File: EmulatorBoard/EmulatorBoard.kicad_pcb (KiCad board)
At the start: 2 copper layers, 106.9 x 59.3 mm, 25 parts, among them J2 Screw_Terminal_01x10, J3 Screw_Terminal_01x02, Q1 BC338, Q2 IRF740, Q3 IRF740, Q4 IRF740, Q5 IRF740, Q6 BC338, U1 TC4424, U2 TC4424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

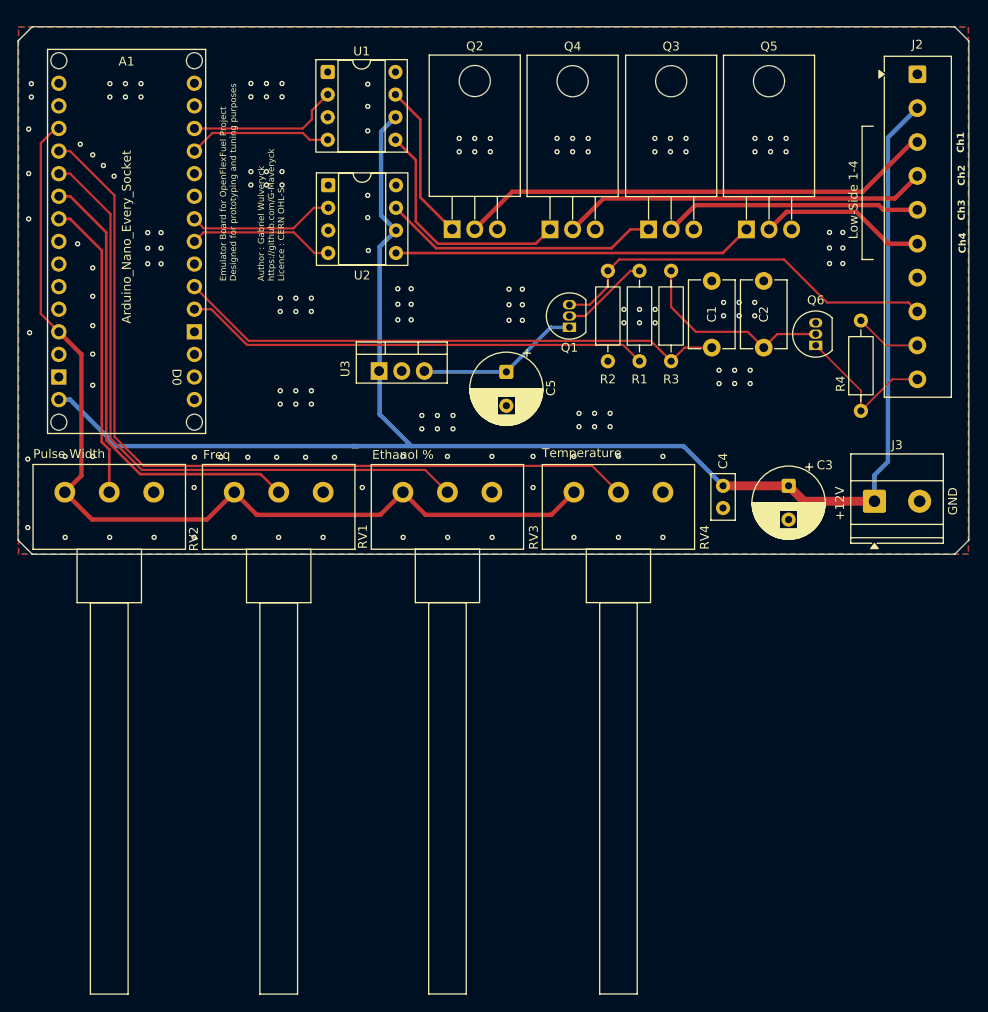
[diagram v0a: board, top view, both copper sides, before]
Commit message: Updated and sourced EmulatoBoard (DevBoard)
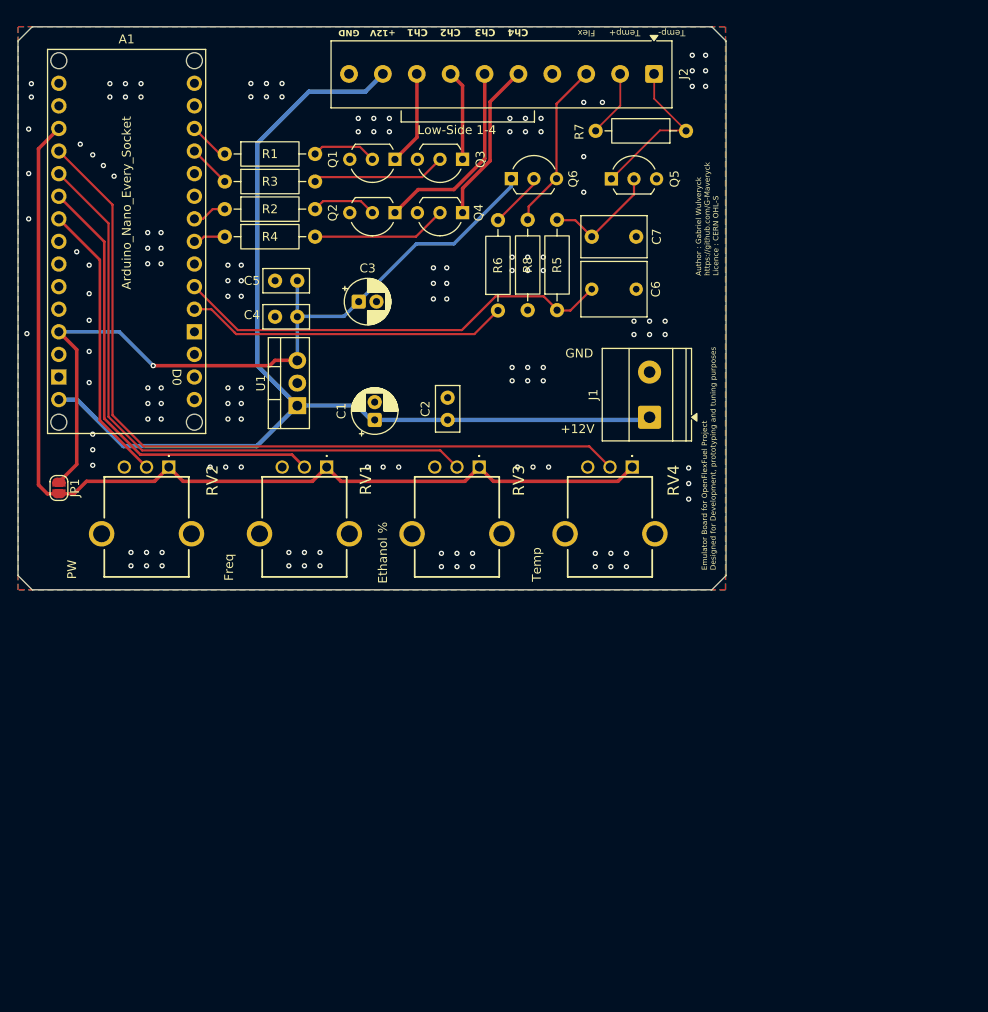
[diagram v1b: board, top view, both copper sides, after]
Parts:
- removed J3: Screw_Terminal_01x02, TerminalBlock_Phoenix:TerminalBlock_Phoenix_MKDS-1,5-2-5.08_1x02_P5.08mm_Horizontal
- removed the RV1 at (66.7, 97.0)
- removed U2: TC4424, Package_DIP:DIP-8_W7.62mm_Socket
- removed U3: LM7805_TO220, Package_TO_SOT_THT:TO-220-3_Vertical
- added C1: 10uF, Capacitor_THT:CP_Radial_D5.0mm_P2.00mm, F.Cu at (82.5, 88.9)
- added C2: 1nF, Capacitor_THT:C_Disc_D5.0mm_W2.5mm_P2.50mm, F.Cu at (90.7, 88.9)
- added J1: Screw_Terminal_01x02, TerminalBlock_Phoenix:TerminalBlock_Phoenix_MKDS-1,5-2-5.08_1x02_P5.08mm_Horizontal, F.Cu at (113.4, 88.6)
- added JP1: SolderJumper_2_Open, Jumper:SolderJumper-2_P1.3mm_Open_RoundedPad1.0x1.5mm, F.Cu at (47.0, 96.5)
- added R1: 1k, Resistor_THT:R_Axial_DIN0207_L6.3mm_D2.5mm_P10.16mm_Horizontal, F.Cu at (65.6, 59.0)
- added R5: 1k, Resistor_THT:R_Axial_DIN0207_L6.3mm_D2.5mm_P10.16mm_Horizontal, F.Cu at (103.0, 76.6)
- added R7: 1k, Resistor_THT:R_Axial_DIN0207_L6.3mm_D2.5mm_P10.16mm_Horizontal, F.Cu at (117.5, 56.4)
- added R8: 1k, Resistor_THT:R_Axial_DIN0207_L6.3mm_D2.5mm_P10.16mm_Horizontal, F.Cu at (99.7, 76.6)
- added RV4: 100k Lin, OpenFlex_FootPrint_Lib:PTN091V100115K1B, F.Cu at (108.5, 100.2)
- C3: footprint Capacitor_THT:CP_Radial_D8.0mm_P3.80mm -> Capacitor_THT:CP_Radial_D5.0mm_P2.00mm
- C5: value 10uF -> 100nF; footprint Capacitor_THT:CP_Radial_D8.0mm_P3.80mm -> Capacitor_THT:C_Disc_D5.0mm_W2.5mm_P2.50mm
- C6: renamed from C1; footprint Capacitor_THT:C_Disc_D7.5mm_W5.0mm_P7.50mm -> Capacitor_THT:C_Rect_L7.2mm_W6.0mm_P5.00mm
- C7: renamed from C2; footprint Capacitor_THT:C_Disc_D7.5mm_W5.0mm_P7.50mm -> Capacitor_THT:C_Rect_L7.2mm_W4.5mm_P5.00mm_FKS2_FKP2_MKS2_MKP2
- Q1, Q6: value BC338 -> 2N2222A; footprint Package_TO_SOT_THT:TO-92_Inline -> Package_TO_SOT_THT:TO-92L_Inline_Wide
- Q2, Q3, Q4, Q5: value IRF740 -> 2N2222A; footprint Package_TO_SOT_THT:TO-220-3_Horizontal_TabDown -> Package_TO_SOT_THT:TO-92L_Inline_Wide
- RV1: renamed from RV4; footprint Potentiometer_THT:Potentiometer_Omeg_PC16BU_Horizontal -> OpenFlex_FootPrint_Lib:PTN091V100115K1B
- RV2, RV3: footprint Potentiometer_THT:Potentiometer_Omeg_PC16BU_Horizontal -> OpenFlex_FootPrint_Lib:PTN091V100115K1B
- U1: value TC4424 -> LM7805_TO220; footprint Package_DIP:DIP-8_W7.62mm_Socket -> Package_TO_SOT_THT:TO-220-3_Vertical
- moved R4 74.2 mm to (65.6, 68.3), turned to 0 degrees
- moved R3 54.1 mm to (65.6, 62.1), turned to 0 degrees
- moved C3 52.6 mm to (80.7, 75.6), turned to 0 degrees
- moved C4 51.5 mm to (73.8, 77.3), turned to 180 degrees
- moved R2 46.3 mm to (65.6, 65.2), turned to 0 degrees
- moved Q6 39.0 mm to (97.9, 61.8), turned to 0 degrees
- moved U1 37.7 mm to (73.8, 87.3), turned to 90 degrees
- moved RV1 31.0 mm to (74.1, 100.2), turned to 180 degrees
- moved J2 29.6 mm to (113.9, 50.0), turned to 180 degrees
- moved Q1 27.2 mm to (84.8, 59.6), turned to 180 degrees
- moved C5 25.6 mm to (73.8, 73.2), turned to 180 degrees
- moved C7 23.0 mm to (106.9, 68.3), turned to 0 degrees
- moved Q3 22.3 mm to (92.4, 59.6), turned to 180 degrees
- moved R6 16.9 mm to (96.4, 76.6)
- moved Q5 16.2 mm to (109.1, 61.8)
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- renumbered R1 to R6
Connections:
- A1 pad 5V: +5V -> VDD
- A1 pad AREF: +5V -> /AREF_Pin
- C3 pad 1: +12V -> VDD
- C4 pad 1: +12V -> VDD
- C7 pad 1: Net-(Q6-B) -> Net-(Q5-B)
- J2 pad 1: GND -> Temp_-
- J2 pad 10: Temp_- -> GND
- J2 pad 2: +12V -> Temp_+
- J2 pad 3: /INJ_CH1 -> Flex_SNSR_Signal
- J2 pad 4: /INJ_CH2 -> unconnected-(J2-Pin_4-Pad4)
- J2 pad 5: /INJ_CH3 -> /INJ_CH4
- J2 pad 6: /INJ_CH4 -> /INJ_CH3
- J2 pad 7: unconnected-(J2-Pin_7-Pad7) -> /INJ_CH2
- J2 pad 8: Flex_SNSR_Signal -> /INJ_CH1
- J2 pad 9: Temp_+ -> +12V
- Q1 pad 1: VDD -> /INJ_CH1
- Q1 pad 3: Flex_SNSR_Signal -> GND
- Q2 pad 1: Net-(Q2-G) -> /INJ_CH3
- Q2 pad 2: /INJ_CH1 -> Net-(Q2-B)
- Q3 pad 1: Net-(Q3-G) -> /INJ_CH2
- Q3 pad 2: /INJ_CH3 -> Net-(Q3-B)
- Q4 pad 1: Net-(Q4-G) -> /INJ_CH4
- Q4 pad 2: /INJ_CH2 -> Net-(Q4-B)
- Q5 pad 1: Net-(Q5-G) -> Temp_-
- Q5 pad 2: /INJ_CH4 -> Net-(Q5-B)
- Q6 pad 1: Temp_- -> VDD
- Q6 pad 3: GND -> Flex_SNSR_Signal
- R2 pad 1: GND -> /GD_CH3
- R2 pad 2: Flex_SNSR_Signal -> Net-(Q2-B)
- R3 pad 1: /MCU_D3 -> /GD_CH2
- R3 pad 2: Net-(Q6-B) -> Net-(Q3-B)
- R4 pad 1: Temp_- -> /GD_CH4
- R4 pad 2: Temp_+ -> Net-(Q4-B)
- R6 pad 2: Net-(Q1-B) -> Net-(Q6-B)
- RV1 pad 1: +5V -> /AREF_Pin
- RV1 pad 2: /Temp_Pot -> /FREQ_Pot
- RV2 pad 1: +5V -> /AREF_Pin
- RV3 pad 1: +5V -> /AREF_Pin
- U1 pad 1: unconnected-(U1-NC-Pad1) -> +12V
- U1 pad 2: /GD_CH1 -> GND
- U1 pad 3: GND -> VDD
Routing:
- net /AREF_Pin: track 0.00 -> 113.8 mm
- net +5V: track 108.6 -> 0.00 mm
- net VDD: track 18.4 -> 87.2 mm, vias 0 -> 1
- net +12V: track 184.1 -> 120.0 mm
- net /INJ_CH1: track 54.0 -> 10.6 mm
- net Net-(Q5-G): track 40.5 -> 0.00 mm
- net Net-(Q3-G): track 31.2 -> 0.00 mm
- net /INJ_CH2: track 42.0 -> 10.9 mm
- net Net-(Q4-G): track 26.9 -> 0.00 mm
- net Flex_SNSR_Signal: track 44.7 -> 19.2 mm
- net Net-(Q2-G): track 17.8 -> 0.00 mm
- net Net-(Q6-B): track 22.8 -> 6.34 mm
- net /MCU_D2: track 52.5 -> 36.4 mm
- net Net-(Q4-B): track 0.00 -> 15.2 mm
- net Net-(Q3-B): track 0.00 -> 15.1 mm
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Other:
- board size 106.9 x 59.3 mm -> 79.6 x 63.3 mm
- board text added: "Emulator Board for OpenFlexFuel Project Designed for Development, prototyping and tuning purposes"
- board text added: "Flex"
- board text added: "PW"
- board text added: "Temp"
- board text added: "Temp+"
- board text added: "Temp-"
- board text removed: "Emulator Board for OpenFlexFuel Project Designed for prototyping and tuning purposes"
- board text removed: "Pulse Width"
- board text removed: "Temperature"

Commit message: Updated BOM
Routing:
- net /AREF_Pin: track 113.8 -> 116.3 mm
- net +12V: track 120.0 -> 120.5 mm
- net GND: vias 137 -> 168
